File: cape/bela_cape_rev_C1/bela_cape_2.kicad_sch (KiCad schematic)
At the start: 16 parts, among them IC6 TSV524xIQ4T, IC7 TSV524xIQ4T, IC8 ADS8168

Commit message: More C1 cape routing
(cherry picked from commit db7d999e21b46c22925661ce0002776775f31ffd)
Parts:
- added TP1: TestPoint, TestPoint:TestPoint_THTPad_D2.0mm_Drill1.0mm, symbol Connector:TestPoint
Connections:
- net GND: no longer C22.1, C23.1, C24.1, C25.1, C26.2, C27.2, C28.2, C29.2, C30.2, C53.1, IC6.11 (V-), IC6.17 (EP), IC7.11 (V-), IC7.17 (EP), IC8.1 (GND), IC8.21 (GND), IC8.31 (GND), IC8.33 (GND), IC8.4 (REFM), IC8.8 (AIN-COM)
- net ANALOG_REF renamed REFP
- net REFP: now also TP1.1
- new net GNDA: C22.1, C23.1, C24.1, C25.1, C26.2, C27.2, C28.2, C29.2, C30.2, C53.1, IC6.11 (V-), IC6.17 (EP), IC7.11 (V-), IC7.17 (EP), IC8.1 (GND), IC8.21 (GND), IC8.31 (GND), IC8.33 (GND), IC8.4 (REFM)
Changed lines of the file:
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@@
   (junction (at 71.12 73.66) (diameter 0) (color 0 0 0 0)
   )
+  (junction (at 120.65 49.53) (diameter 0) (color 0 0 0 0)
+  )
   (junction (at 189.23 93.98) (diameter 0) (color 0 0 0 0)
   )
@@
   (junction (at 71.12 31.75) (diameter 0) (color 0 0 0 0)
   )
-  (junction (at 119.38 49.53) (diameter 0) (color 0 0 0 0)
-  )
   (junction (at 129.54 34.29) (diameter 0) (color 0 0 0 0)
   )
@@
   (junction (at 189.23 96.52) (diameter 0) (color 0 0 0 0)
   )
+  (junction (at 119.38 100.33) (diameter 0) (color 0 0 0 0)
+  )
   (junction (at 189.23 88.9) (diameter 0) (color 0 0 0 0)
   )
@@
     (stroke (width 0) (type default) (color 0 0 0 0))
   )
+  (wire (pts (xy 120.65 49.53) (xy 123.19 49.53))
+    (stroke (width 0) (type default) (color 0 0 0 0))
+  )
   (wire (pts (xy 53.34 85.09) (xy 55.88 85.09))
     (stroke (width 0) (type default) (color 0 0 0 0))
@@
     (stroke (width 0) (type default) (color 0 0 0 0))
   )
-  (wire (pts (xy 116.84 49.53) (xy 119.38 49.53))
+  (wire (pts (xy 116.84 49.53) (xy 120.65 49.53))
     (stroke (width 0) (type default) (color 0 0 0 0))
   )
@@
     (stroke (width 0) (type default) (color 0 0 0 0))
   )
+  (wire (pts (xy 199.39 87.63) (xy 209.55 87.63))
+    (stroke (width 0) (type default) (color 0 0 0 0))
+  )
   (wire (pts (xy 38.1 71.12) (xy 50.8 71.12))
     (stroke (width 0) (type default) (color 0 0 0 0))
@@
     (stroke (width 0) (type default) (color 0 0 0 0))
   )
-  (wire (pts (xy 119.38 49.53) (xy 123.19 49.53))
-    (stroke (width 0) (type default) (color 0 0 0 0))
-  )
   (wire (pts (xy 182.88 74.93) (xy 187.96 74.93))
     (stroke (width 0) (type default) (color 0 0 0 0))
@@
   )
   (wire (pts (xy 50.8 99.06) (xy 55.88 99.06))
-    (stroke (width 0) (type default) (color 0 0 0 0))
-  )
-  (wire (pts (xy 38.1 88.9) (xy 44.45 88.9))
     (stroke (width 0) (type default) (color 0 0 0 0))
   )
@@
     (effects (font (size 1.27 1.27)) (justify left bottom))
   )
-  (label "REFP" (at 39.37 88.9 0)
+  (label "REFP" (at 199.39 87.63 0)
     (effects (font (size 1.27 1.27)) (justify left bottom))
   )
@@
   )
   (hierarchical_label "ANALOG7" (shape input) (at 38.1 83.82 180)
-    (effects (font (size 1.27 1.27)) (justify right))
-  )
-  (hierarchical_label "ANALOG_REF" (shape output) (at 38.1 88.9 180)
     (effects (font (size 1.27 1.27)) (justify right))
   )
@@
     (pin "3")
   )
+  (symbol (lib_id "power:GNDA") (at 189.23 100.33 0) (unit 1)
+    (in_bom yes) (on_board yes) (fields_autoplaced)
+    (property "Reference" "#PWR?" (id 0) (at 189.23 106.68 0)
+      (effects (font (size 1.27 1.27)) hide)
+    )
+    (property "Value" "GNDA" (id 1) (at 189.23 104.8925 0))
+    (property "Footprint" "" (id 2) (at 189.23 100.33 0)
+      (effects (font (size 1.27 1.27)) hide)
+    )
+    (property "Datasheet" "" (id 3) (at 189.23 100.33 0)
+      (effects (font (size 1.27 1.27)) hide)
+    )
+    (pin "1")
+  )
+  (symbol (lib_id "power:GNDA") (at 167.64 45.72 0) (unit 1)
+    (in_bom yes) (on_board yes) (fields_autoplaced)
+    (property "Reference" "#PWR?" (id 0) (at 167.64 52.07 0)
+      (effects (font (size 1.27 1.27)) hide)
+    )
+    (property "Value" "GNDA" (id 1) (at 167.64 50.2825 0))
+    (property "Footprint" "" (id 2) (at 167.64 45.72 0)
+      (effects (font (size 1.27 1.27)) hide)
+    )
+    (property "Datasheet" "" (id 3) (at 167.64 45.72 0)
+      (effects (font (size 1.27 1.27)) hide)
+    )
+    (pin "1")
+  )
   (symbol (lib_id "Device:R_Pack04") (at 177.8 77.47 270) (unit 1)
     (in_bom yes) (on_board yes) (fields_autoplaced)
@@
     (pin "2")
   )
-  (symbol (lib_id "power:GND") (at 147.32 105.41 0) (unit 1)
-    (in_bom yes) (on_board yes) (fields_autoplaced)
-    (property "Reference" "#PWR0125" (id 0) (at 147.32 111.76 0)
-      (effects (font (size 1.27 1.27)) hide)
-    )
-    (property "Value" "GND" (id 1) (at 147.32 109.9725 0))
-    (property "Footprint" "" (id 2) (at 147.32 105.41 0)
-      (effects (font (size 1.27 1.27)) hide)
-    )
-    (property "Datasheet" "" (id 3) (at 147.32 105.41 0)
-      (effects (font (size 1.27 1.27)) hide)
-    )
-    (pin "1")
-  )
-  (symbol (lib_id "power:GND") (at 119.38 49.53 0) (unit 1)
-    (in_bom yes) (on_board yes) (fields_autoplaced)
-    (property "Reference" "#PWR0131" (id 0) (at 119.38 55.88 0)
-      (effects (font (size 1.27 1.27)) hide)
-    )
-    (property "Value" "GND" (id 1) (at 119.38 54.0925 0))
-    (property "Footprint" "" (id 2) (at 119.38 49.53 0)
-      (effects (font (size 1.27 1.27)) hide)
-    )
-    (property "Datasheet" "" (id 3) (at 119.38 49.53 0)
-      (effects (font (size 1.27 1.27)) hide)
-    )
-    (pin "1")
-  )
   (symbol (lib_id "Amplifier_Operational:TSV524xIQ4T") (at 63.5 87.63 0) (unit 4)
     (in_bom yes) (on_board yes) (fields_autoplaced)
@@
     (pin "3")
   )
+  (symbol (lib_id "power:GNDA") (at 120.65 49.53 0) (unit 1)
+    (in_bom yes) (on_board yes) (fields_autoplaced)
+    (property "Reference" "#PWR?" (id 0) (at 120.65 55.88 0)
+      (effects (font (size 1.27 1.27)) hide)
+    )
+    (property "Value" "GNDA" (id 1) (at 120.65 54.0925 0))
+    (property "Footprint" "" (id 2) (at 120.65 49.53 0)
+      (effects (font (size 1.27 1.27)) hide)
+    )
+    (property "Datasheet" "" (id 3) (at 120.65 49.53 0)
+      (effects (font (size 1.27 1.27)) hide)
+    )
+    (pin "1")
+  )
   (symbol (lib_id "power:GND") (at 172.72 67.31 0) (unit 1)
     (in_bom yes) (on_board yes) (fields_autoplaced)
@@
     (pin "2")
   )
-  (symbol (lib_id "power:GND") (at 119.4308 100.33 0) (unit 1)
-    (in_bom yes) (on_board yes) (fields_autoplaced)
-    (property "Reference" "#PWR0126" (id 0) (at 119.4308 106.68 0)
-      (effects (font (size 1.27 1.27)) hide)
-    )
-    (property "Value" "GND" (id 1) (at 119.4308 104.8925 0))
-    (property "Footprint" "" (id 2) (at 119.4308 100.33 0)
-      (effects (font (size 1.27 1.27)) hide)
-    )
-    (property "Datasheet" "" (id 3) (at 119.4308 100.33 0)
+  (symbol (lib_id "Connector:TestPoint") (at 209.55 87.63 0) (unit 1)
+    (in_bom yes) (on_board yes) (fields_autoplaced)
+    (property "Reference" "TP1" (id 0) (at 210.947 83.4933 0)
+      (effects (font (size 1.27 1.27)) (justify left))
+    )
+    (property "Value" "TestPoint" (id 1) (at 210.947 86.0302 0)
+      (effects (font (size 1.27 1.27)) (justify left))
+    )
+    (property "Footprint" "TestPoint:TestPoint_THTPad_D2.0mm_Drill1.0mm" (id 2) (at 214.63 87.63 0)
+      (effects (font (size 1.27 1.27)) hide)
+    )
+    (property "Datasheet" "~" (id 3) (at 214.63 87.63 0)
+      (effects (font (size 1.27 1.27)) hide)
+    )
+    (pin "1")
+  )
+  (symbol (lib_id "power:GNDA") (at 147.32 105.41 0) (unit 1)
+    (in_bom yes) (on_board yes) (fields_autoplaced)
+    (property "Reference" "#PWR?" (id 0) (at 147.32 111.76 0)
+      (effects (font (size 1.27 1.27)) hide)
+    )
+    (property "Value" "GNDA" (id 1) (at 147.32 109.9725 0))
+    (property "Footprint" "" (id 2) (at 147.32 105.41 0)
+      (effects (font (size 1.27 1.27)) hide)
+    )
+    (property "Datasheet" "" (id 3) (at 147.32 105.41 0)
       (effects (font (size 1.27 1.27)) hide)
     )
@@
     (pin "9")
   )
-  (symbol (lib_id "power:GND") (at 189.23 100.33 0) (unit 1)
-    (in_bom yes) (on_board yes) (fields_autoplaced)
-    (property "Reference" "#PWR0129" (id 0) (at 189.23 106.68 0)
-      (effects (font (size 1.27 1.27)) hide)
-    )
-    (property "Value" "GND" (id 1) (at 189.23 104.8925 0))
-    (property "Footprint" "" (id 2) (at 189.23 100.33 0)
-      (effects (font (size 1.27 1.27)) hide)
-    )
-    (property "Datasheet" "" (id 3) (at 189.23 100.33 0)
+  (symbol (lib_id "power:GNDA") (at 119.38 100.33 0) (unit 1)
+    (in_bom yes) (on_board yes) (fields_autoplaced)
+    (property "Reference" "#PWR?" (id 0) (at 119.38 106.68 0)
+      (effects (font (size 1.27 1.27)) hide)
+    )
+    (property "Value" "GNDA" (id 1) (at 119.38 104.8925 0))
+    (property "Footprint" "" (id 2) (at 119.38 100.33 0)
+      (effects (font (size 1.27 1.27)) hide)
+    )
+    (property "Datasheet" "" (id 3) (at 119.38 100.33 0)
       (effects (font (size 1.27 1.27)) hide)
     )
@@
     (pin "2")
   )
-  (symbol (lib_id "power:GND") (at 167.64 45.72 0) (unit 1)
-    (in_bom yes) (on_board yes) (fields_autoplaced)
-    (property "Reference" "#PWR0127" (id 0) (at 167.64 52.07 0)
-      (effects (font (size 1.27 1.27)) hide)
-    )
-    (property "Value" "GND" (id 1) (at 167.64 50.2825 0))
-    (property "Footprint" "" (id 2) (at 167.64 45.72 0)
-      (effects (font (size 1.27 1.27)) hide)
-    )
-    (property "Datasheet" "" (id 3) (at 167.64 45.72 0)
-      (effects (font (size 1.27 1.27)) hide)
-    )
-    (pin "1")
-  )
 )

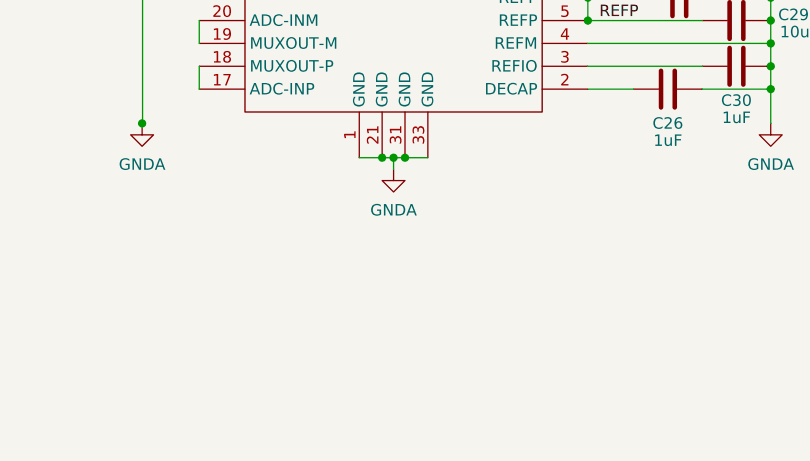
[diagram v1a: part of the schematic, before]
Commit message: Further routing on C1 cape
(cherry picked from commit 232a25b01e013bf194cdc3a343766aa7b43870aa)
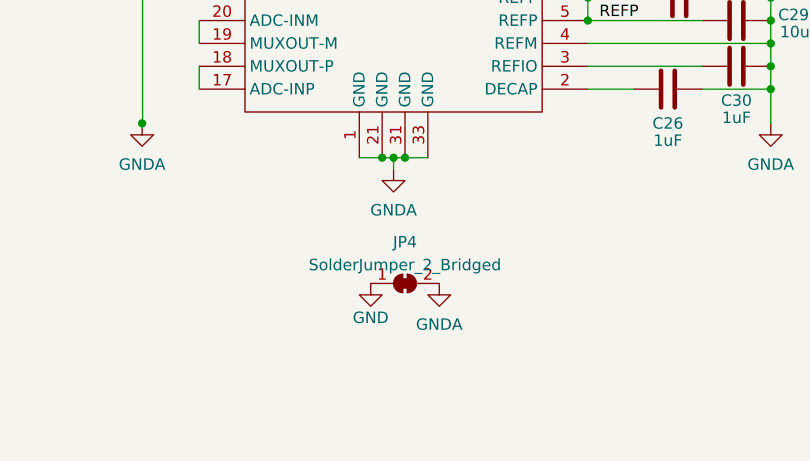
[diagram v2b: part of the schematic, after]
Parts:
- added JP4: SolderJumper_2_Bridged, Jumper:SolderJumper-2_P1.3mm_Bridged_Pad1.0x1.5mm, symbol Jumper:SolderJumper_2_Bridged
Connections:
- net GND: now also JP4.1 (A)
- net GNDA: now also JP4.2 (B)
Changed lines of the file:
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@@
     (pin "3")
+  )
+  (symbol (lib_id "Jumper:SolderJumper_2_Bridged") (at 148.59 118.11 0) (unit 1)
+    (in_bom yes) (on_board yes) (fields_autoplaced)
+    (property "Reference" "JP4" (id 0) (at 148.59 113.5212 0))
+    (property "Value" "SolderJumper_2_Bridged" (id 1) (at 148.59 116.0581 0))
+    (property "Footprint" "Jumper:SolderJumper-2_P1.3mm_Bridged_Pad1.0x1.5mm" (id 2) (at 148.59 118.11 0)
+      (effects (font (size 1.27 1.27)) hide)
+    )
+    (property "Datasheet" "~" (id 3) (at 148.59 118.11 0)
+      (effects (font (size 1.27 1.27)) hide)
+    )
+    (pin "1")
+    (pin "2")
   )
   (symbol (lib_id "Amplifier_Operational:TSV524xIQ4T") (at 63.5 101.6 0) (unit 3)
@@
   (symbol (lib_id "power:GNDA") (at 189.23 100.33 0) (unit 1)
     (in_bom yes) (on_board yes) (fields_autoplaced)
-    (property "Reference" "#PWR?" (id 0) (at 189.23 106.68 0)
+    (property "Reference" "#PWR0131" (id 0) (at 189.23 106.68 0)
       (effects (font (size 1.27 1.27)) hide)
     )
@@
   (symbol (lib_id "power:GNDA") (at 167.64 45.72 0) (unit 1)
     (in_bom yes) (on_board yes) (fields_autoplaced)
-    (property "Reference" "#PWR?" (id 0) (at 167.64 52.07 0)
+    (property "Reference" "#PWR0126" (id 0) (at 167.64 52.07 0)
       (effects (font (size 1.27 1.27)) hide)
     )
@@
   (symbol (lib_id "power:GNDA") (at 120.65 49.53 0) (unit 1)
     (in_bom yes) (on_board yes) (fields_autoplaced)
-    (property "Reference" "#PWR?" (id 0) (at 120.65 55.88 0)
+    (property "Reference" "#PWR0146" (id 0) (at 120.65 55.88 0)
       (effects (font (size 1.27 1.27)) hide)
     )
@@
     (pin "2")
   )
+  (symbol (lib_id "power:GND") (at 144.78 118.11 0) (mirror y) (unit 1)
+    (in_bom yes) (on_board yes)
+    (property "Reference" "#PWR0168" (id 0) (at 144.78 124.46 0)
+      (effects (font (size 1.27 1.27)) hide)
+    )
+    (property "Value" "GND" (id 1) (at 144.78 121.92 0))
+    (property "Footprint" "" (id 2) (at 144.78 118.11 0)
+      (effects (font (size 1.27 1.27)) hide)
+    )
+    (property "Datasheet" "" (id 3) (at 144.78 118.11 0)
+      (effects (font (size 1.27 1.27)) hide)
+    )
+    (pin "1")
+  )
   (symbol (lib_id "Connector:TestPoint") (at 209.55 87.63 0) (unit 1)
     (in_bom yes) (on_board yes) (fields_autoplaced)
@@
     (pin "1")
   )
+  (symbol (lib_id "power:GNDA") (at 152.4 118.11 0) (unit 1)
+    (in_bom yes) (on_board yes)
+    (property "Reference" "#PWR0167" (id 0) (at 152.4 124.46 0)
+      (effects (font (size 1.27 1.27)) hide)
+    )
+    (property "Value" "GNDA" (id 1) (at 152.4 122.6725 0))
+    (property "Footprint" "" (id 2) (at 152.4 118.11 0)
+      (effects (font (size 1.27 1.27)) hide)
+    )
+    (property "Datasheet" "" (id 3) (at 152.4 118.11 0)
+      (effects (font (size 1.27 1.27)) hide)
+    )
+    (pin "1")
+  )
   (symbol (lib_id "power:GNDA") (at 147.32 105.41 0) (unit 1)
     (in_bom yes) (on_board yes) (fields_autoplaced)
-    (property "Reference" "#PWR?" (id 0) (at 147.32 111.76 0)
+    (property "Reference" "#PWR0127" (id 0) (at 147.32 111.76 0)
       (effects (font (size 1.27 1.27)) hide)
     )
@@
   (symbol (lib_id "power:GNDA") (at 119.38 100.33 0) (unit 1)
     (in_bom yes) (on_board yes) (fields_autoplaced)
-    (property "Reference" "#PWR?" (id 0) (at 119.38 106.68 0)
-      (effects (font (size 1.27 1.27)) hide)
-    )
+    (property "Reference" "#PWR0129" (id 0) (at 119.38 106.68 0)
+      (effects (font (size 1.27 1.27)) hide)
+    )

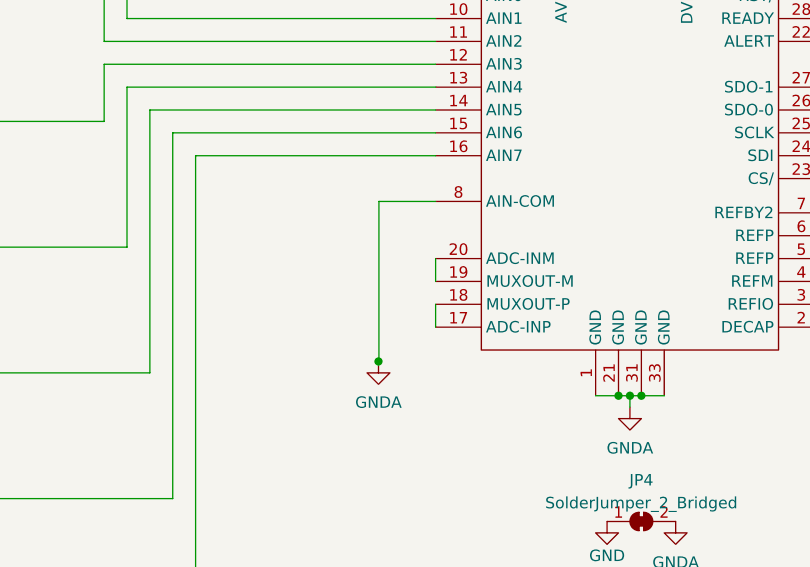
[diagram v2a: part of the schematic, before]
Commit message: First complete routing of C1 cape
(cherry picked from commit 8c5092941a0b3ec42f55098733fd0108b2086674)
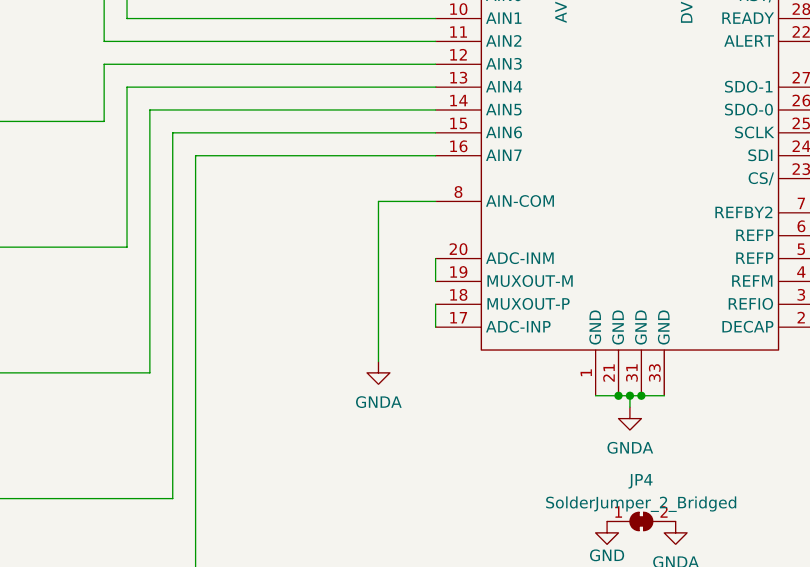
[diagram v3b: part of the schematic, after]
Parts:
- JP4: footprint Jumper:SolderJumper-2_P1.3mm_Bridged_Pad1.0x1.5mm -> Bela:SolderJumper2_with_mask
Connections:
- net GNDA: now also IC8.8 (AIN-COM)
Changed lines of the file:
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@@
   (junction (at 189.23 96.52) (diameter 0) (color 0 0 0 0)
   )
-  (junction (at 119.38 100.33) (diameter 0) (color 0 0 0 0)
-  )
   (junction (at 189.23 88.9) (diameter 0) (color 0 0 0 0)
   )
@@
     (stroke (width 0) (type default) (color 0 0 0 0))
   )
-  (wire (pts (xy 125.73 82.55) (xy 119.4308 82.55))
-    (stroke (width 0) (type default) (color 0 0 0 0))
-  )
-  (wire (pts (xy 119.4308 82.55) (xy 119.4308 100.33))
+  (wire (pts (xy 119.38 82.55) (xy 125.73 82.55))
     (stroke (width 0) (type default) (color 0 0 0 0))
   )
@@
   )
   (wire (pts (xy 45.72 127) (xy 45.72 83.82))
+    (stroke (width 0) (type default) (color 0 0 0 0))
+  )
+  (wire (pts (xy 119.38 82.55) (xy 119.38 100.33))
     (stroke (width 0) (type default) (color 0 0 0 0))
   )
@@
     (property "Reference" "JP4" (id 0) (at 148.59 113.5212 0))
     (property "Value" "SolderJumper_2_Bridged" (id 1) (at 148.59 116.0581 0))
-    (property "Footprint" "Jumper:SolderJumper-2_P1.3mm_Bridged_Pad1.0x1.5mm" (id 2) (at 148.59 118.11 0)
-      (effects (font (size 1.27 1.27)) hide)
-    )
+    (property "Footprint" "Bela:SolderJumper2_with_mask" (id 2) (at 148.59 118.11 0)
+      (effects (font (size 1.27 1.27)) hide)
+    )

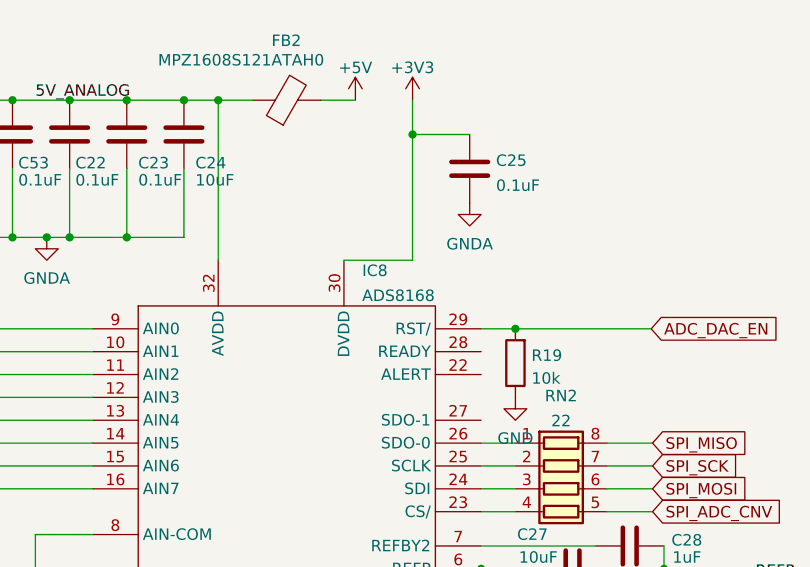
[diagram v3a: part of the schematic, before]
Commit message: C1 cape: clean up bottom silkscreen
(cherry picked from commit 7c02b20f8f7a862246e5856b6fa8015b8ad6464b)
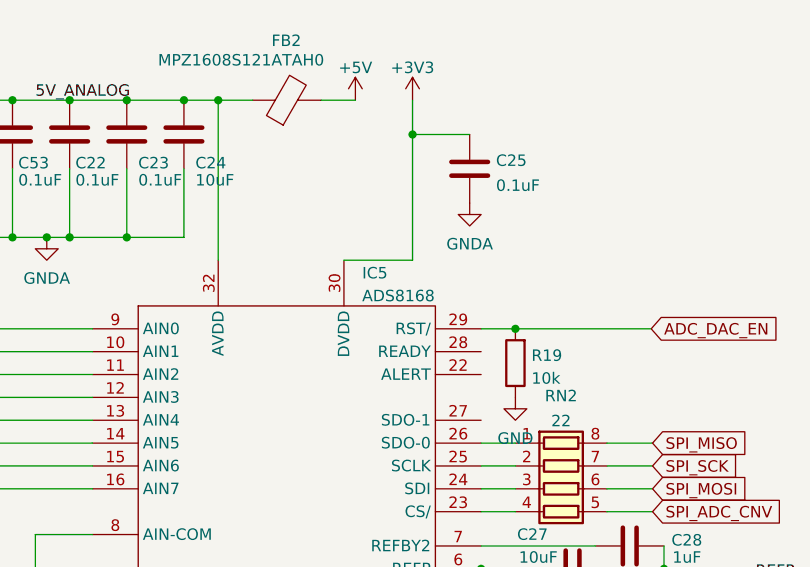
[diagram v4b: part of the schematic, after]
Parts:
- renumbered IC8 to IC5
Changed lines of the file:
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@@
   (symbol (lib_id "Bela:ADS8168") (at 148.59 48.26 0) (unit 1)
     (in_bom yes) (on_board yes) (fields_autoplaced)
-    (property "Reference" "IC8" (id 0) (at 155.6894 53.2343 0)
+    (property "Reference" "IC5" (id 0) (at 155.6894 53.501 0)
       (effects (font (size 1.27 1.27)) (justify left))
     )
-    (property "Value" "ADS8168" (id 1) (at 155.6894 56.0094 0)
+    (property "Value" "ADS8168" (id 1) (at 155.6894 56.0379 0)
       (effects (font (size 1.27 1.27)) (justify left))
     )

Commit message: Bela cape C1: renumber components
(cherry picked from commit 6ebfe9c44bb7559ffb4c9dbd092e49803523e6a1)
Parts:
- renumbered C53 to C43, C22 to C44, C23 to C45, C24 to C46, C25 to C47, C28 to C48, C27 to C49, C29 to C50, C30 to C51, C26 to C52, FB2 to FB3, IC6 to IC7, IC7 to IC8, IC5 to IC9, JP4 to JP5, R19 to R45
